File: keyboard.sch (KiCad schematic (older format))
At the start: 24 parts

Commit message: Key Matrix
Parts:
- removed D? (x4): SOD-123, symbol Device:D_Small
- removed MX? (x4): MX-LED, symbol MX_Alps_Hybrid:MX-LED
- added R?: 33k, symbol Device:R_Small
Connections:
- net labels added: COL0, COL1, COL10, COL11, COL12, COL13, COL14, COL15, COL16, COL17, COL2, COL3, COL4, COL5, COL6, COL7, COL8, COL9, ROW0, ROW1, ROW2, ROW3, ROW4, ROW5
- wire segments 56 -> 51
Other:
- moved on the sheet: C?, F?, P?, R?, SW?, U?, Y?

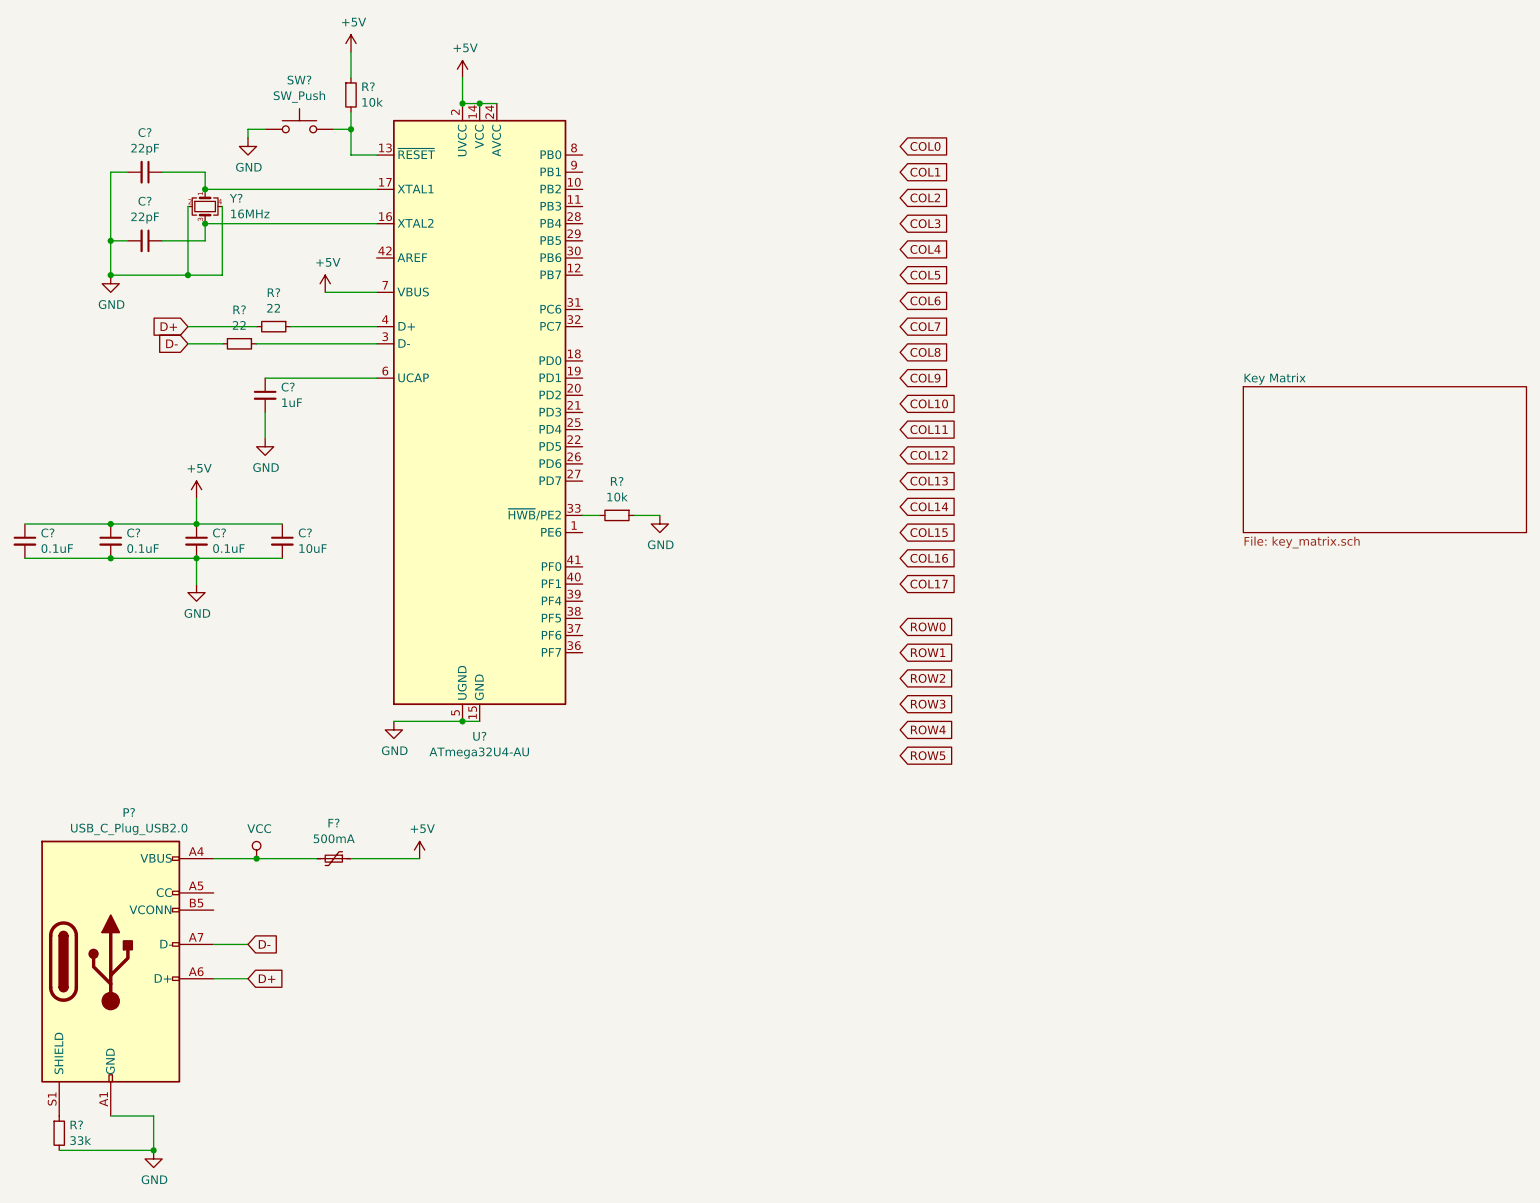
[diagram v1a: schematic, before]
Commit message: Schematic & Footprint bindings
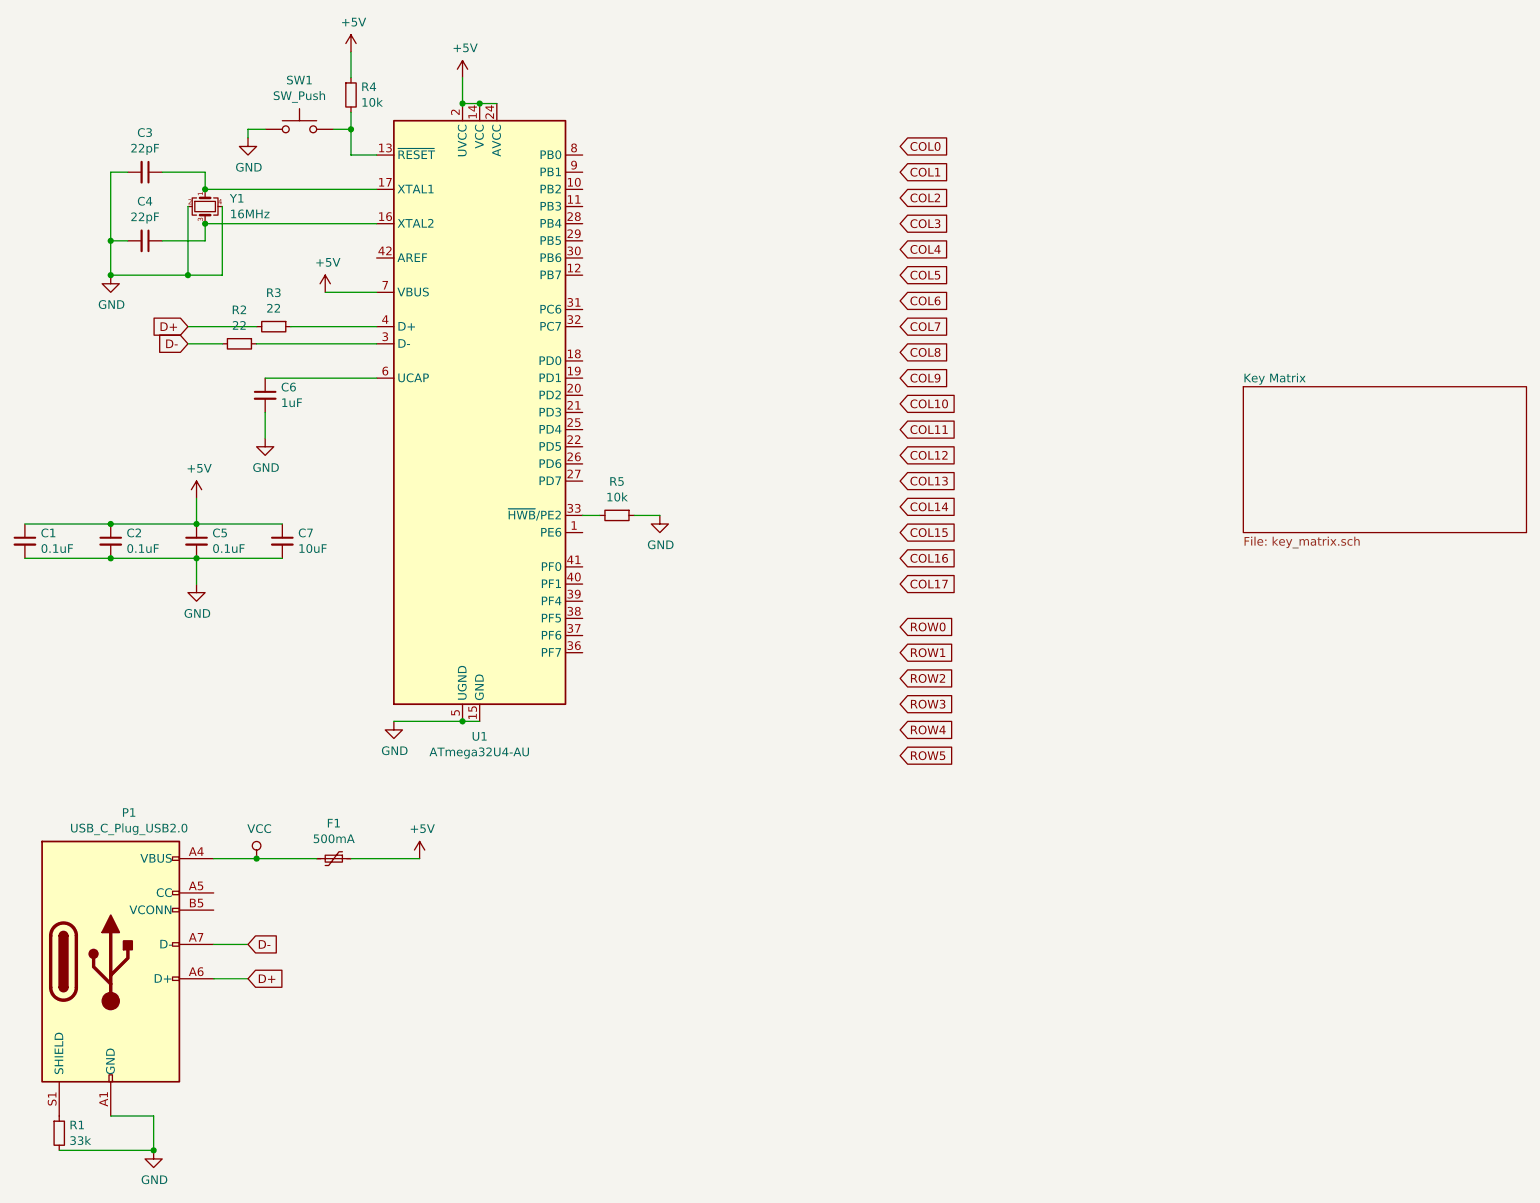
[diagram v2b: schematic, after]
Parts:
- C1, C2, C3, C4, C5, C6, C7: renamed from C?; footprint (none) -> Capacitor_SMD:C_0805_2012Metric
- F1: renamed from F?; footprint (none) -> Fuse:Fuse_1206_3216Metric
- P1: renamed from P?; footprint (none) -> Type-C:USB_C_GCT_USB4085
- R1, R2, R3, R4, R5: renamed from R?; footprint (none) -> Resistor_SMD:R_0805_2012Metric
- SW1: renamed from SW?; footprint (none) -> random-keyboard-parts:SKQG-1155865
- Y1: renamed from Y?; footprint (none) -> Crystal:Crystal_SMD_3225-4Pin_3.2x2.5mm
- gave numbers to parts that had none: 1
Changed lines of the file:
@@
 	3200 1000 3200 850
 $Comp
-L MCU_Microchip_ATmega:ATmega32U4-AU U?
+L MCU_Microchip_ATmega:ATmega32U4-AU U1
 U 1 1 5D8CB7C1
 P 3300 2800
-F 0 "U?" H 3300 911 50  0000 C CNN
+F 0 "U1" H 3300 911 50  0000 C CNN
 F 1 "ATmega32U4-AU" H 3300 820 50  0000 C CNN
 F 2 "Package_QFP:TQFP-44_10x10mm_P0.8mm" H 3300 2800 50  0001 C CIN
@@
 $EndComp
 $Comp
-L Device:R_Small R?
+L Device:R_Small R5
 U 1 1 5D8D1835
 P 4100 3400
-F 0 "R?" V 3904 3400 50  0000 C CNN
+F 0 "R5" V 3904 3400 50  0000 C CNN
 F 1 "10k" V 3995 3400 50  0000 C CNN
-F 2 "" H 4100 3400 50  0001 C CNN
+F 2 "Resistor_SMD:R_0805_2012Metric" H 4100 3400 50  0001 C CNN
 F 3 "~" H 4100 3400 50  0001 C CNN
 	1    4100 3400
@@
 	4200 3400 4350 3400
 $Comp
-L Device:R_Small R?
+L Device:R_Small R3
 U 1 1 5D8D4621
 P 2100 2300
-F 0 "R?" V 1904 2300 50  0000 C CNN
+F 0 "R3" V 1904 2300 50  0000 C CNN
 F 1 "22" V 1995 2300 50  0000 C CNN
-F 2 "" H 2100 2300 50  0001 C CNN
+F 2 "Resistor_SMD:R_0805_2012Metric" H 2100 2300 50  0001 C CNN
 F 3 "~" H 2100 2300 50  0001 C CNN
 	1    2100 2300
@@
 $EndComp
 $Comp
-L Device:R_Small R?
+L Device:R_Small R2
 U 1 1 5D8D4F73
 P 1900 2400
-F 0 "R?" V 1704 2400 50  0000 C CNN
+F 0 "R2" V 1704 2400 50  0000 C CNN
 F 1 "22" V 1795 2400 50  0000 C CNN
-F 2 "" H 1900 2400 50  0001 C CNN
+F 2 "Resistor_SMD:R_0805_2012Metric" H 1900 2400 50  0001 C CNN
 F 3 "~" H 1900 2400 50  0001 C CNN
 	1    1900 2400
@@
 	2700 2400 2000 2400
 $Comp
-L Device:C_Small C?
+L Device:C_Small C6
 U 1 1 5D8D5FD8
 P 2050 2700
-F 0 "C?" H 2142 2746 50  0000 L CNN
+F 0 "C6" H 2142 2746 50  0000 L CNN
 F 1 "1uF" H 2142 2655 50  0000 L CNN
-F 2 "" H 2050 2700 50  0001 C CNN
+F 2 "Capacitor_SMD:C_0805_2012Metric" H 2050 2700 50  0001 C CNN
 F 3 "~" H 2050 2700 50  0001 C CNN
 	1    2050 2700
@@
 $EndComp
 $Comp
-L Device:C_Small C?
+L Device:C_Small C5
 U 1 1 5D8D71E4
 P 1650 3550
-F 0 "C?" H 1742 3596 50  0000 L CNN
+F 0 "C5" H 1742 3596 50  0000 L CNN
 F 1 "0.1uF" H 1742 3505 50  0000 L CNN
-F 2 "" H 1650 3550 50  0001 C CNN
+F 2 "Capacitor_SMD:C_0805_2012Metric" H 1650 3550 50  0001 C CNN
 F 3 "~" H 1650 3550 50  0001 C CNN
 	1    1650 3550
@@
 $EndComp
 $Comp
-L Device:C_Small C?
+L Device:C_Small C2
 U 1 1 5D8D7A31
 P 1150 3550
-F 0 "C?" H 1242 3596 50  0000 L CNN
+F 0 "C2" H 1242 3596 50  0000 L CNN
 F 1 "0.1uF" H 1242 3505 50  0000 L CNN
-F 2 "" H 1150 3550 50  0001 C CNN
+F 2 "Capacitor_SMD:C_0805_2012Metric" H 1150 3550 50  0001 C CNN
 F 3 "~" H 1150 3550 50  0001 C CNN
 	1    1150 3550
@@
 $EndComp
 $Comp
-L Device:C_Small C?
+L Device:C_Small C7
 U 1 1 5D8D7C60
 P 2150 3550
-F 0 "C?" H 2242 3596 50  0000 L CNN
+F 0 "C7" H 2242 3596 50  0000 L CNN
 F 1 "10uF" H 2242 3505 50  0000 L CNN
-F 2 "" H 2150 3550 50  0001 C CNN
+F 2 "Capacitor_SMD:C_0805_2012Metric" H 2150 3550 50  0001 C CNN
 F 3 "~" H 2150 3550 50  0001 C CNN
 	1    2150 3550
@@
 $EndComp
 $Comp
-L Device:C_Small C?
+L Device:C_Small C1
 U 1 1 5D8D7EF5
 P 650 3550
-F 0 "C?" H 742 3596 50  0000 L CNN
+F 0 "C1" H 742 3596 50  0000 L CNN
 F 1 "0.1uF" H 742 3505 50  0000 L CNN
-F 2 "" H 650 3550 50  0001 C CNN
+F 2 "Capacitor_SMD:C_0805_2012Metric" H 650 3550 50  0001 C CNN
 F 3 "~" H 650 3550 50  0001 C CNN
 	1    650  3550
@@
 	2400 2100 2700 2100
 $Comp
-L Device:Crystal_GND24_Small Y?
+L Device:Crystal_GND24_Small Y1
 U 1 1 5D8DD184
 P 1700 1600
-F 0 "Y?" V 1654 1744 50  0000 L CNN
+F 0 "Y1" V 1654 1744 50  0000 L CNN
 F 1 "16MHz" V 1745 1744 50  0000 L CNN
-F 2 "" H 1700 1600 50  0001 C CNN
+F 2 "Crystal:Crystal_SMD_3225-4Pin_3.2x2.5mm" H 1700 1600 50  0001 C CNN
 F 3 "~" H 1700 1600 50  0001 C CNN
 	1    1700 1600
@@
 	2700 1700 1700 1700
 $Comp
-L Device:C_Small C?
+L Device:C_Small C3
 U 1 1 5D8E220B
 P 1350 1400
-F 0 "C?" V 1121 1400 50  0000 C CNN
+F 0 "C3" V 1121 1400 50  0000 C CNN
 F 1 "22pF" V 1212 1400 50  0000 C CNN
-F 2 "" H 1350 1400 50  0001 C CNN
+F 2 "Capacitor_SMD:C_0805_2012Metric" H 1350 1400 50  0001 C CNN
 F 3 "~" H 1350 1400 50  0001 C CNN
 	1    1350 1400
@@
 $EndComp
 $Comp
-L Device:C_Small C?
+L Device:C_Small C4
 U 1 1 5D8E2E48
 P 1350 1800
-F 0 "C?" V 1121 1800 50  0000 C CNN
+F 0 "C4" V 1121 1800 50  0000 C CNN
 F 1 "22pF" V 1212 1800 50  0000 C CNN
-F 2 "" H 1350 1800 50  0001 C CNN
+F 2 "Capacitor_SMD:C_0805_2012Metric" H 1350 1800 50  0001 C CNN
 F 3 "~" H 1350 1800 50  0001 C CNN
 	1    1350 1800
@@
 Connection ~ 1600 2000
 $Comp
-L Switch:SW_Push SW?
+L Switch:SW_Push SW1
 U 1 1 5D8E66DE
 P 2250 1150
-F 0 "SW?" H 2250 1435 50  0000 C CNN
+F 0 "SW1" H 2250 1435 50  0000 C CNN
 F 1 "SW_Push" H 2250 1344 50  0000 C CNN
-F 2 "" H 2250 1350 50  0001 C CNN
+F 2 "random-keyboard-parts:SKQG-1155865" H 2250 1350 50  0001 C CNN
 F 3 "~" H 2250 1350 50  0001 C CNN
 	1    2250 1150
@@
 	1950 1150 2050 1150
 $Comp
-L Device:R_Small R?
+L Device:R_Small R4
 U 1 1 5D8E8DB9
 P 2550 950
-F 0 "R?" H 2609 996 50  0000 L CNN
+F 0 "R4" H 2609 996 50  0000 L CNN
 F 1 "10k" H 2609 905 50  0000 L CNN
-F 2 "" H 2550 950 50  0001 C CNN
+F 2 "Resistor_SMD:R_0805_2012Metric" H 2550 950 50  0001 C CNN
 F 3 "~" H 2550 950 50  0001 C CNN
 	1    2550 950
@@
 $EndComp
 $Comp
-L Device:R_Small R?
+L Device:R_Small R1
 U 1 1 5D8EA5AB
 P 850 7000
-F 0 "R?" H 909 7046 50  0000 L CNN
+F 0 "R1" H 909 7046 50  0000 L CNN
 F 1 "33k" H 909 6955 50  0000 L CNN
-F 2 "" H 850 7000 50  0001 C CNN
+F 2 "Resistor_SMD:R_0805_2012Metric" H 850 7000 50  0001 C CNN
 F 3 "~" H 850 7000 50  0001 C CNN
 	1    850  7000
@@
 	1750 5900 1950 5900
 $Comp
-L Connector:USB_C_Plug_USB2.0 P?
+L Connector:USB_C_Plug_USB2.0 P1
 U 1 1 5D8EC3D3
 P 1150 6000
-F 0 "P?" H 1257 6867 50  0000 C CNN
+F 0 "P1" H 1257 6867 50  0000 C CNN
 F 1 "USB_C_Plug_USB2.0" H 1257 6776 50  0000 C CNN
-F 2 "" H 1300 6000 50  0001 C CNN
+F 2 "Type-C:USB_C_GCT_USB4085" H 1300 6000 50  0001 C CNN
 F 3 "https://www.usb.org/sites/default/files/documents/usb_type-c.zip" H 1300 6000 50  0001 C CNN
 	1    1150 6000
@@
 $EndComp
 $Comp
-L Device:Polyfuse_Small F?
+L Device:Polyfuse_Small F1
 U 1 1 5D8EE86F
 P 2450 5400
-F 0 "F?" V 2245 5400 50  0000 C CNN
+F 0 "F1" V 2245 5400 50  0000 C CNN
 F 1 "500mA" V 2336 5400 50  0000 C CNN
-F 2 "" H 2500 5200 50  0001 L CNN
+F 2 "Fuse:Fuse_1206_3216Metric" H 2500 5200 50  0001 L CNN
 F 3 "~" H 2450 5400 50  0001 C CNN
 	1    2450 5400

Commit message: Routing & LEDS
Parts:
- added R6: 500, Resistor_SMD:R_0805_2012Metric, symbol Device:R_Small
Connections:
- net COL0: now also U1.19 (PD1)
- net COL1: now also U1.12 (PB7)
- net COL10: now also U1.28 (PB4)
- net COL11: now also U1.27 (PD7)
- net COL12: now also U1.26 (PD6)
- net COL13: now also U1.25 (PD4)
- net COL14: now also U1.11 (PB3)
- net COL15: now also U1.10 (PB2)
- net COL16: now also U1.9 (PB1)
- net COL17: now also U1.8 (PB0)
- net COL2: now also U1.18 (PD0)
- net COL3: now also U1.20 (PD2)
- net COL4: now also U1.21 (PD3)
- net COL5: now also U1.22 (PD5)
- net COL6: now also U1.32 (PC7)
- net COL7: now also U1.31 (PC6)
- net COL8: now also U1.30 (PB6)
- net COL9: now also U1.29 (PB5)
- net ROW0: now also U1.41 (PF0)
- net ROW1: now also U1.40 (PF1)
- net ROW2: now also U1.39 (PF4)
- net ROW3: now also U1.38 (PF5)
- net ROW4: now also U1.37 (PF6)
- net ROW5: now also U1.36 (PF7)
- net at U1.1 (PE6): now also R6.2
- new net LED_DATA: R6.1
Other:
- moved on the sheet: R5

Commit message: Ground Fill, Track Clearances, USB C CC & VCONN
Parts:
- added R7, R8: 5.1k, Resistor_SMD:R_0805_2012Metric, symbol Device:R_Small
- P1: symbol Connector:USB_C_Plug_USB2.0 -> Connector:USB_C_Receptacle_USB2.0
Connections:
- net D+: now also P1.B6 (D+)
- net D-: now also P1.B7 (D-)
- net GND: now also R7.2, R8.2
- net at P1.A5 (CC1): now also R7.1
- net at P1.B5 (CC2): now also R8.1
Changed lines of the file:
@@
 	1750 5900 1950 5900
 $Comp
-L Connector:USB_C_Plug_USB2.0 P1
+L Connector:USB_C_Receptacle_USB2.0 P1
 U 1 1 5D8EC3D3
 P 1150 6000
@@
 Wire Wire Line
 	3900 3400 4450 3400
+$Comp
+L Device:R_Small R7
+U 1 1 5D91C75B
+P 2050 7000
+F 0 "R7" H 2109 7046 50  0000 L CNN
+F 1 "5.1k" H 2109 6955 50  0000 L CNN
+F 2 "Resistor_SMD:R_0805_2012Metric" H 2050 7000 50  0001 C CNN
+F 3 "~" H 2050 7000 50  0001 C CNN
+	1    2050 7000
+	1    0    0    -1
+$EndComp
+Wire Wire Line
+	1400 7100 1800 7100
+Wire Wire Line
+	2050 6900 2050 5600
+Wire Wire Line
+	2050 5600 1750 5600
+$Comp
+L Device:R_Small R8
+U 1 1 5D923014
+P 1800 7000
+F 0 "R8" H 1859 7046 50  0000 L CNN
+F 1 "5.1k" H 1859 6955 50  0000 L CNN
+F 2 "Resistor_SMD:R_0805_2012Metric" H 1800 7000 50  0001 C CNN
+F 3 "~" H 1800 7000 50  0001 C CNN
+	1    1800 7000
+	1    0    0    -1
+$EndComp
+Connection ~ 1800 7100
+Wire Wire Line
+	1800 7100 2050 7100
+Wire Wire Line
+	1800 5700 1750 5700
+Wire Wire Line
+	1800 6900 1800 5700
+Wire Wire Line
+	1750 6000 1750 5900
+Connection ~ 1750 5900
+Wire Wire Line
+	1750 6200 1750 6100
+Connection ~ 1750 6100
 $EndSCHEMATC
